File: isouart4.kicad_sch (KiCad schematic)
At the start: 25 parts, among them J1 USB_B, J2 Conn_01x04, J3 Conn_01x04, J4 Conn_01x04, J5 Conn_01x04, U2 π122U31, U3 AMS1117-3.3, U4 π122U31, U5 π122U31, U6 π122U31

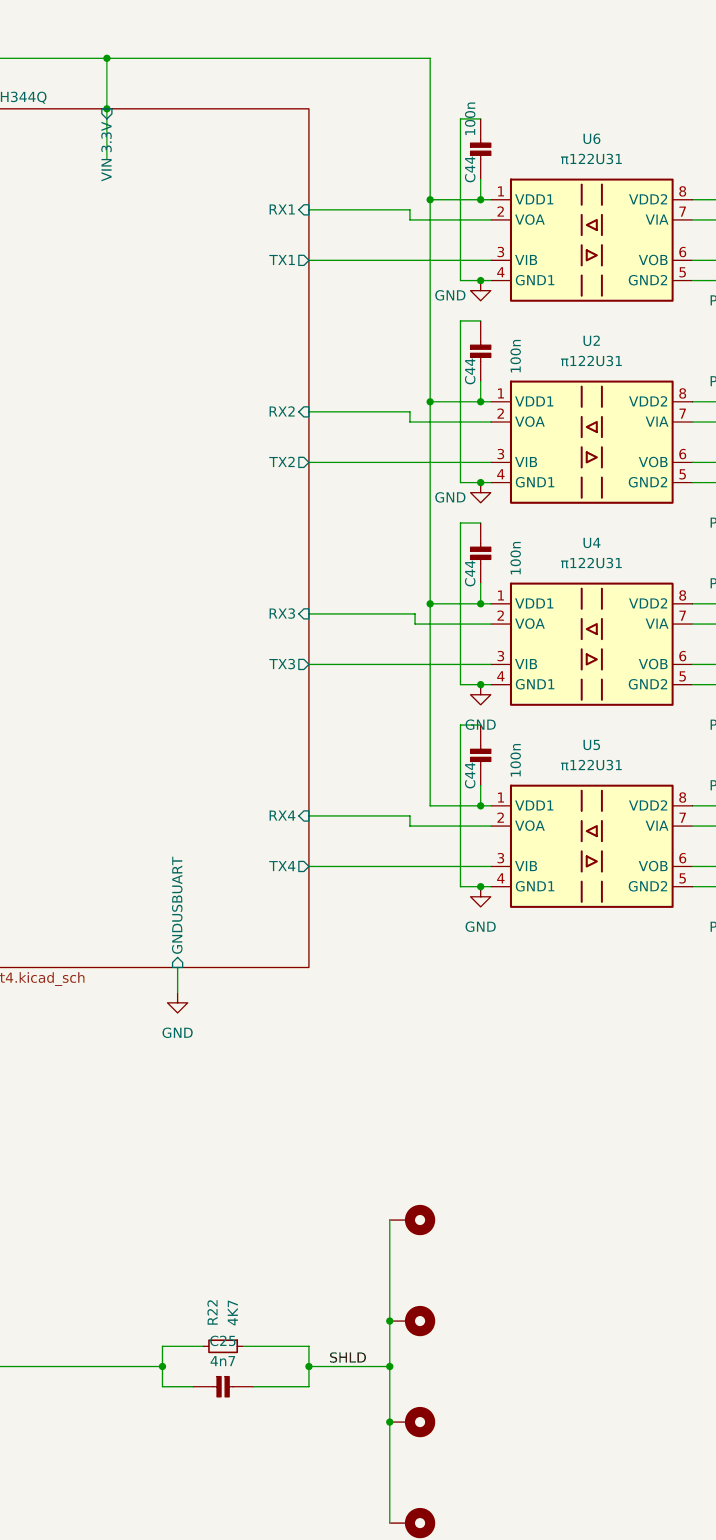
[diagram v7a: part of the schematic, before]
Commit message: Restore 0805 capacitor footprints; Use anotherguse/FuseX copy form isouart4 lib
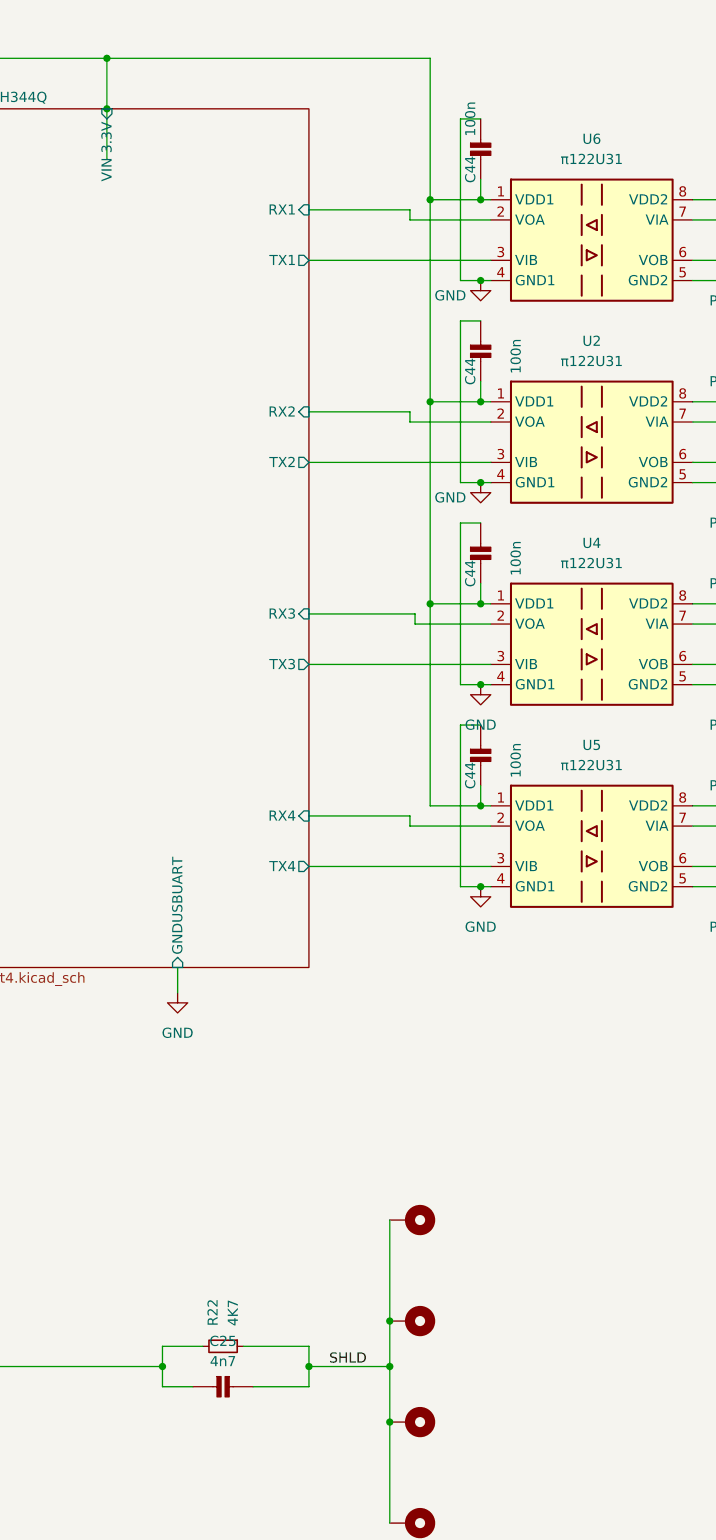
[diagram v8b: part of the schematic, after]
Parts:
- C25, C44: footprint Capacitor_SMD:C_0603_1608Metric_Pad1.08x0.95mm_HandSolder -> Capacitor_SMD:C_0805_2012Metric_Pad1.18x1.45mm_HandSolder
- F1: footprint anotherfuse:FuseX -> isouart4:FuseX
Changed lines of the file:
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@@
       (effects (font (size 1.27 1.27)))
     )
-    (property "Footprint" "Capacitor_SMD:C_0603_1608Metric_Pad1.08x0.95mm_HandSolder" (at 165.735 255.905 0)
+    (property "Footprint" "Capacitor_SMD:C_0805_2012Metric_Pad1.18x1.45mm_HandSolder" (at 165.735 255.905 0)
       (effects (font (size 1.27 1.27)) hide)
     )
@@
       (effects (font (size 1.27 1.27)) (justify right))
     )
-    (property "Footprint" "anotherfuse:FuseX" (at 81.28 109.855 0)
+    (property "Footprint" "isouart4:FuseX" (at 81.28 109.855 0)
       (effects (font (size 1.27 1.27)) hide)
     )
@@
       (effects (font (size 1.27 1.27)))
     )
-    (property "Footprint" "Capacitor_SMD:C_0603_1608Metric_Pad1.08x0.95mm_HandSolder" (at 199.39 177.8 0)
+    (property "Footprint" "Capacitor_SMD:C_0805_2012Metric_Pad1.18x1.45mm_HandSolder" (at 199.39 177.8 0)
       (effects (font (size 1.27 1.27)) hide)
     )
@@
       (effects (font (size 1.27 1.27)))
     )
-    (property "Footprint" "Capacitor_SMD:C_0603_1608Metric_Pad1.08x0.95mm_HandSolder" (at 199.39 127 0)
+    (property "Footprint" "Capacitor_SMD:C_0805_2012Metric_Pad1.18x1.45mm_HandSolder" (at 199.39 127 0)
       (effects (font (size 1.27 1.27)) hide)
     )
@@
       (effects (font (size 1.27 1.27)))
     )
-    (property "Footprint" "Capacitor_SMD:C_0603_1608Metric_Pad1.08x0.95mm_HandSolder" (at 199.39 152.4 0)
+    (property "Footprint" "Capacitor_SMD:C_0805_2012Metric_Pad1.18x1.45mm_HandSolder" (at 199.39 152.4 0)
       (effects (font (size 1.27 1.27)) hide)
     )
@@
       (effects (font (size 1.27 1.27)))
     )
-    (property "Footprint" "Capacitor_SMD:C_0603_1608Metric_Pad1.08x0.95mm_HandSolder" (at 199.39 101.6 0)
-      (effects (font (size 1.27 1.27)) hide)
-    )
+    (property "Footprint" "Capacitor_SMD:C_0805_2012Metric_Pad1.18x1.45mm_HandSolder" (at 199.39 101.6 0)
+      (effects (font (size 1.27 1.27)) hide)
+    )
